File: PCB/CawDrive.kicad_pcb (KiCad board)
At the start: 4 copper layers, 50 x 42 mm, 109 parts, among them CN2 WAFER-SH1.0-6PWB, CN3 WAFER-SH1.0-4PWB, Q10 TPH3R704PL, Q11 TPH3R704PL, Q12 TPH3R704PL, Q7 TPH3R704PL, Q8 TPH3R704PL, Q9 TPH3R704PL, U1 TJA1051T/3/1J, U10 WAFER-SH1.0-2PWB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

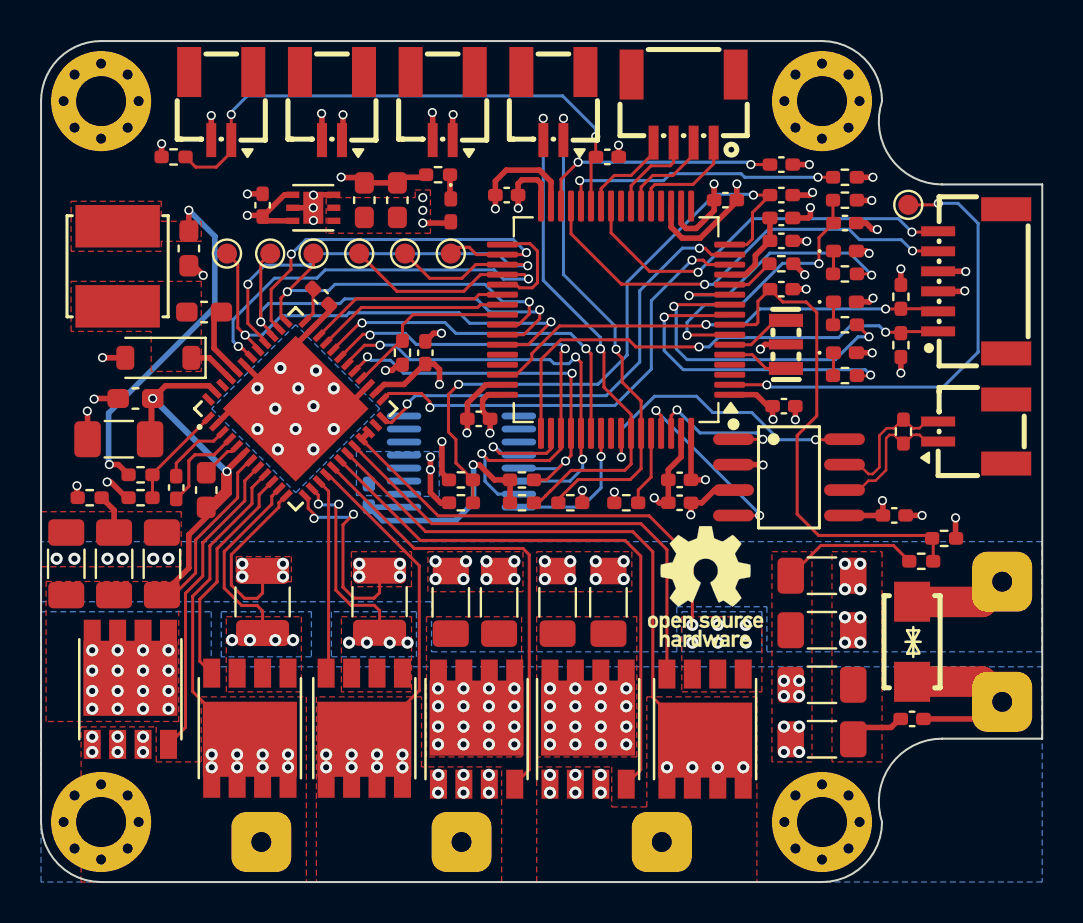
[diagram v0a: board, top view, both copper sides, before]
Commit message: 完成FOC速度闭环控制
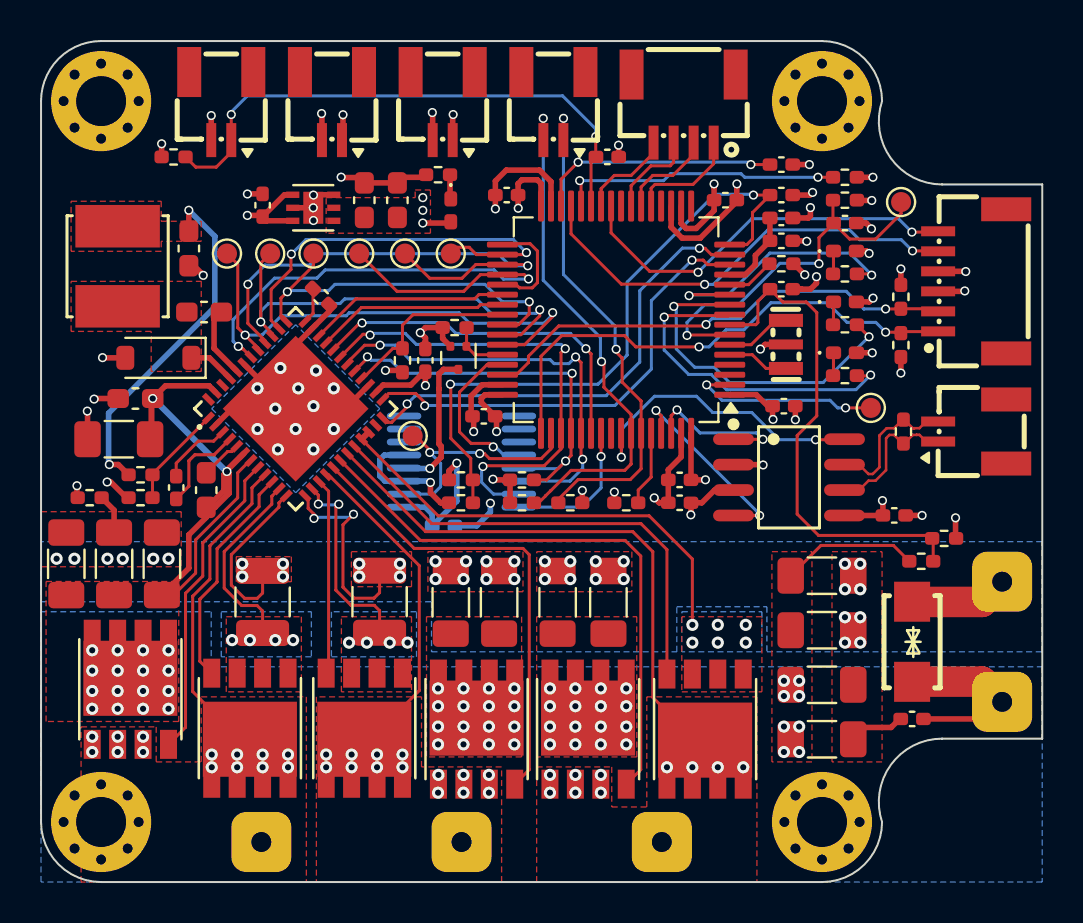
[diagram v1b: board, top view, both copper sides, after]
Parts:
- removed REF**: OSHW-Logo_5.7x6mm_SilkScreen, Symbol:OSHW-Logo_5.7x6mm_SilkScreen
- added Q1: NMOS, Package_TO_SOT_SMD:SOT-723, F.Cu at (140.8, 83.8)
- added R22: 10k, Resistor_SMD:R_0402_1005Metric_Pad0.72x0.64mm_HandSolder, F.Cu at (140.7, 82.3)
- added TP8: TestPoint, TestPoint:TestPoint_Pad_D1.0mm, F.Cu at (162.9, 76.0)
- added TP9: TestPoint, TestPoint:TestPoint_Pad_D1.0mm, F.Cu at (138.6, 87.7)
- moved TP7 10.3 mm to (161.4, 86.3)
- moved C18 4.03 mm to (140.1, 92.2), turned to 180 degrees
- moved C32 0.38 mm to (139.2, 83.9)
- moved R17 0.38 mm to (138.0, 83.9)
- moved C5 0.28 mm to (142.1, 86.7)
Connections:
- U8 pad 44: unconnected-(U8-PA11-Pad44) -> /MT6835_EN
- U8 pad 45: unconnected-(U8-PA12-Pad45) -> /ENCODER_CAL_EN
- U8 pad 50: /ENCODER_CAL_EN -> /ENCODER_OUT
- U9 pad 10: unconnected-(U9-OUT-Pad10) -> /ENCODER_OUT
- U9 pad 12: GND -> Net-(Q1-D)
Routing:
- net Net-(U8-PC13): track 23.5 -> 9.83 mm
- net /ENCODER_OUT: track 0.00 -> 12.3 mm, vias 0 -> 2
- net GND: track 69.1 -> 78.1 mm
- net Net-(Q1-D): track 0.00 -> 7.37 mm, vias 0 -> 1
- net +3.3V: track 52.8 -> 45.7 mm
- net /RESET: track 14.1 -> 18.9 mm
- net /MT6835_EN: track 0.00 -> 2.91 mm
- net /ENCODER_CAL_EN: track 5.34 -> 8.14 mm
- net /SWCLK: track 24.7 -> 25.9 mm
- net /DRV_STA: track 16.2 -> 17.1 mm
- net /TIM1_CH3: track 24.3 -> 25.0 mm
- net /SWDIO: track 23.4 -> 24.1 mm
- net /ENCODER_STA: track 16.5 -> 17.1 mm
- net /SPI3_SCK: track 24.9 -> 24.4 mm

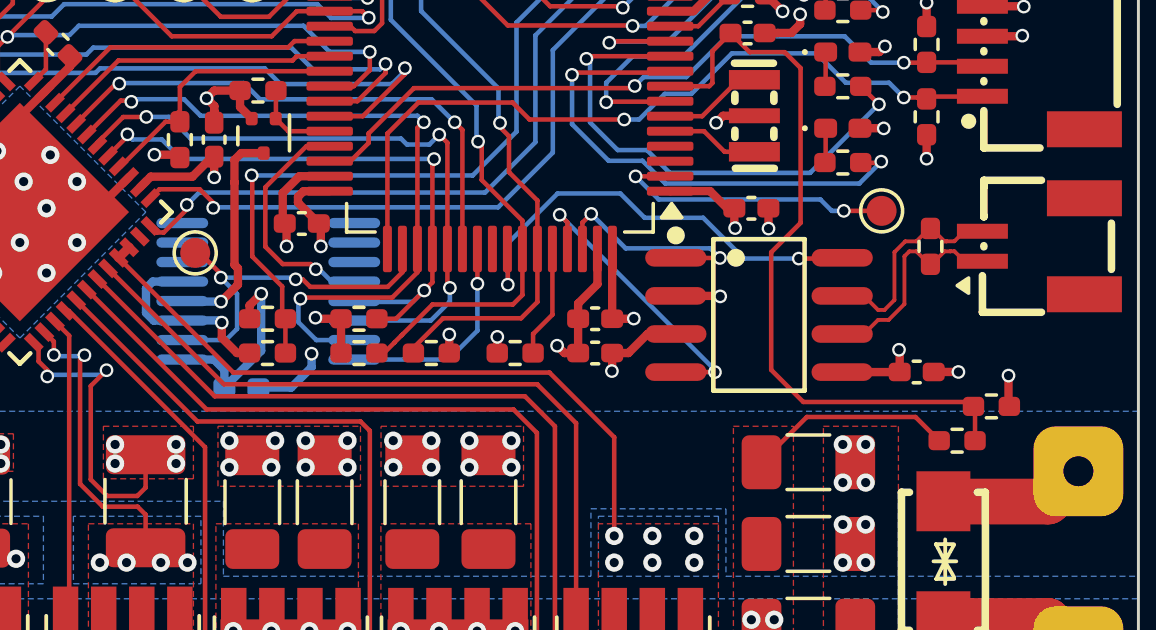
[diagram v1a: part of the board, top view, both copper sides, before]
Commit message: 增加编码器复位功能
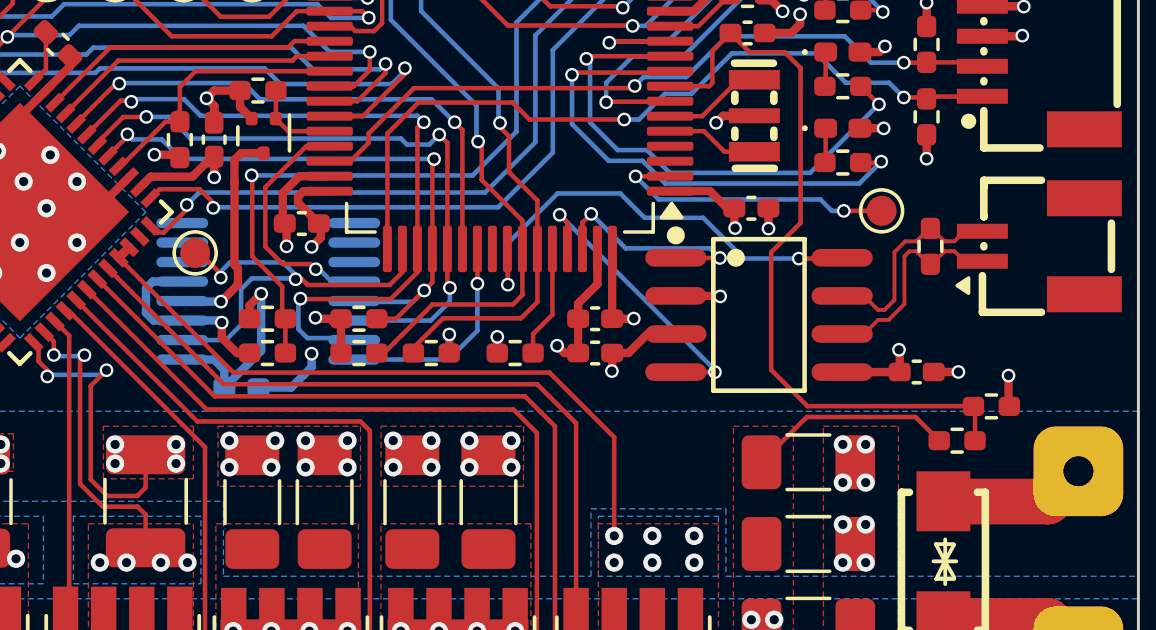
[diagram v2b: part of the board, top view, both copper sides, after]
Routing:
- net /ENCODER_OUT: track 12.3 -> 14.3 mm
